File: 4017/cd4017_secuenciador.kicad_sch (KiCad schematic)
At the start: 20 parts, among them J1 CLK_IN_555, J2 ALIM_EXT, J3 POT1_EXT, J4 POT2_EXT, J5 POT3_EXT, J6 POT4_EXT, J7 JACK_OUT, U1 CD4017BE

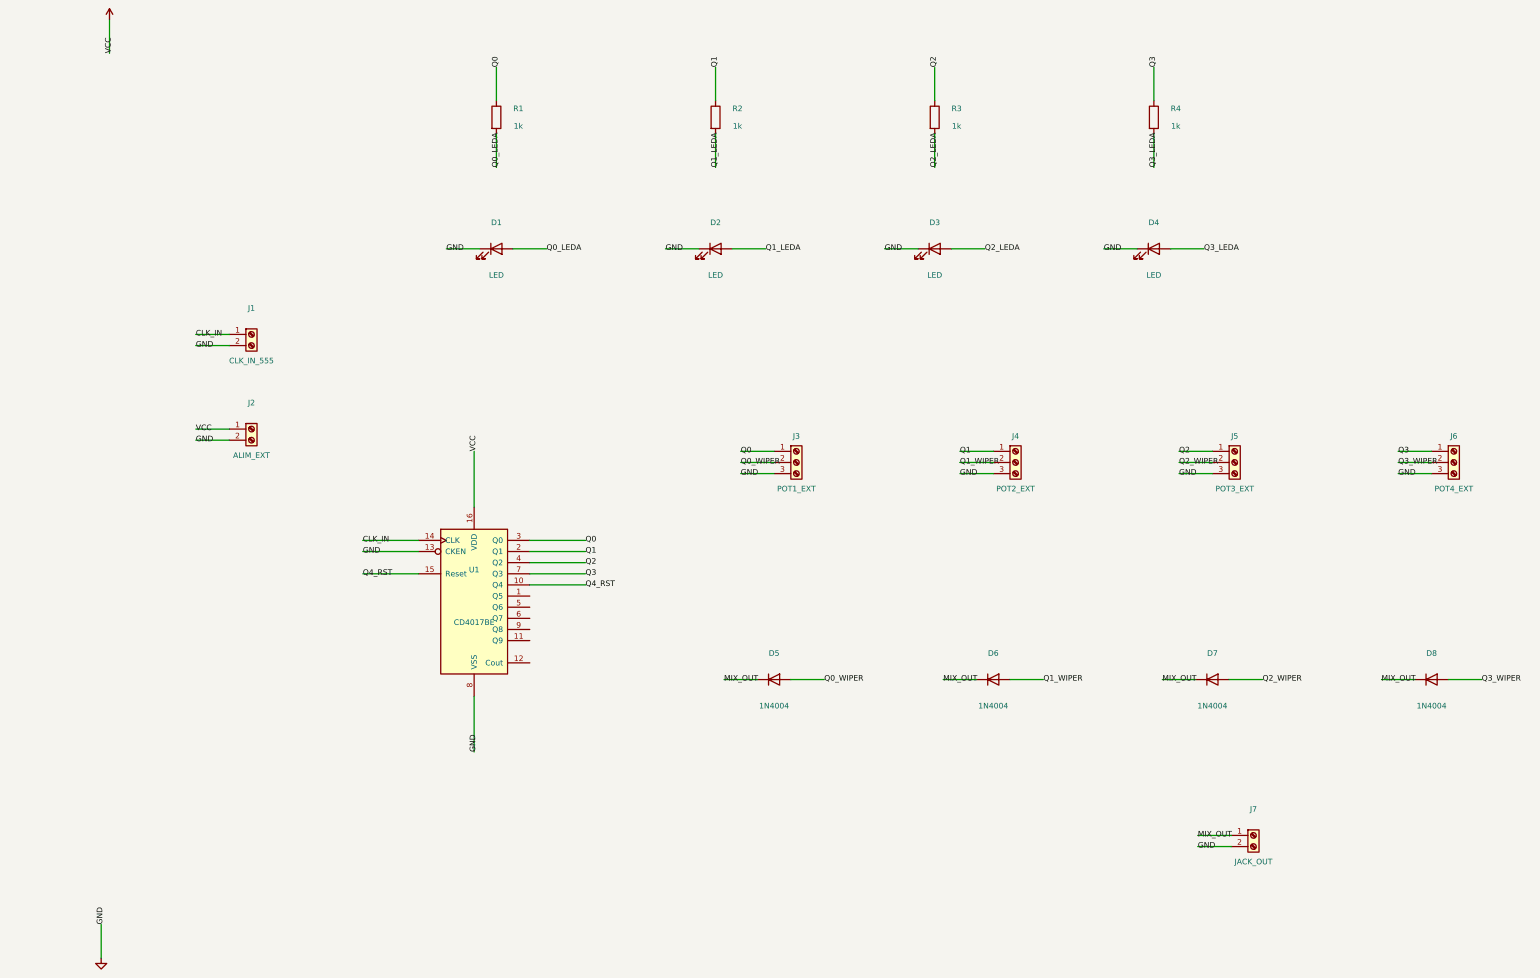
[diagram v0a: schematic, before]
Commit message: enrutado 4017 + correccion esquematico
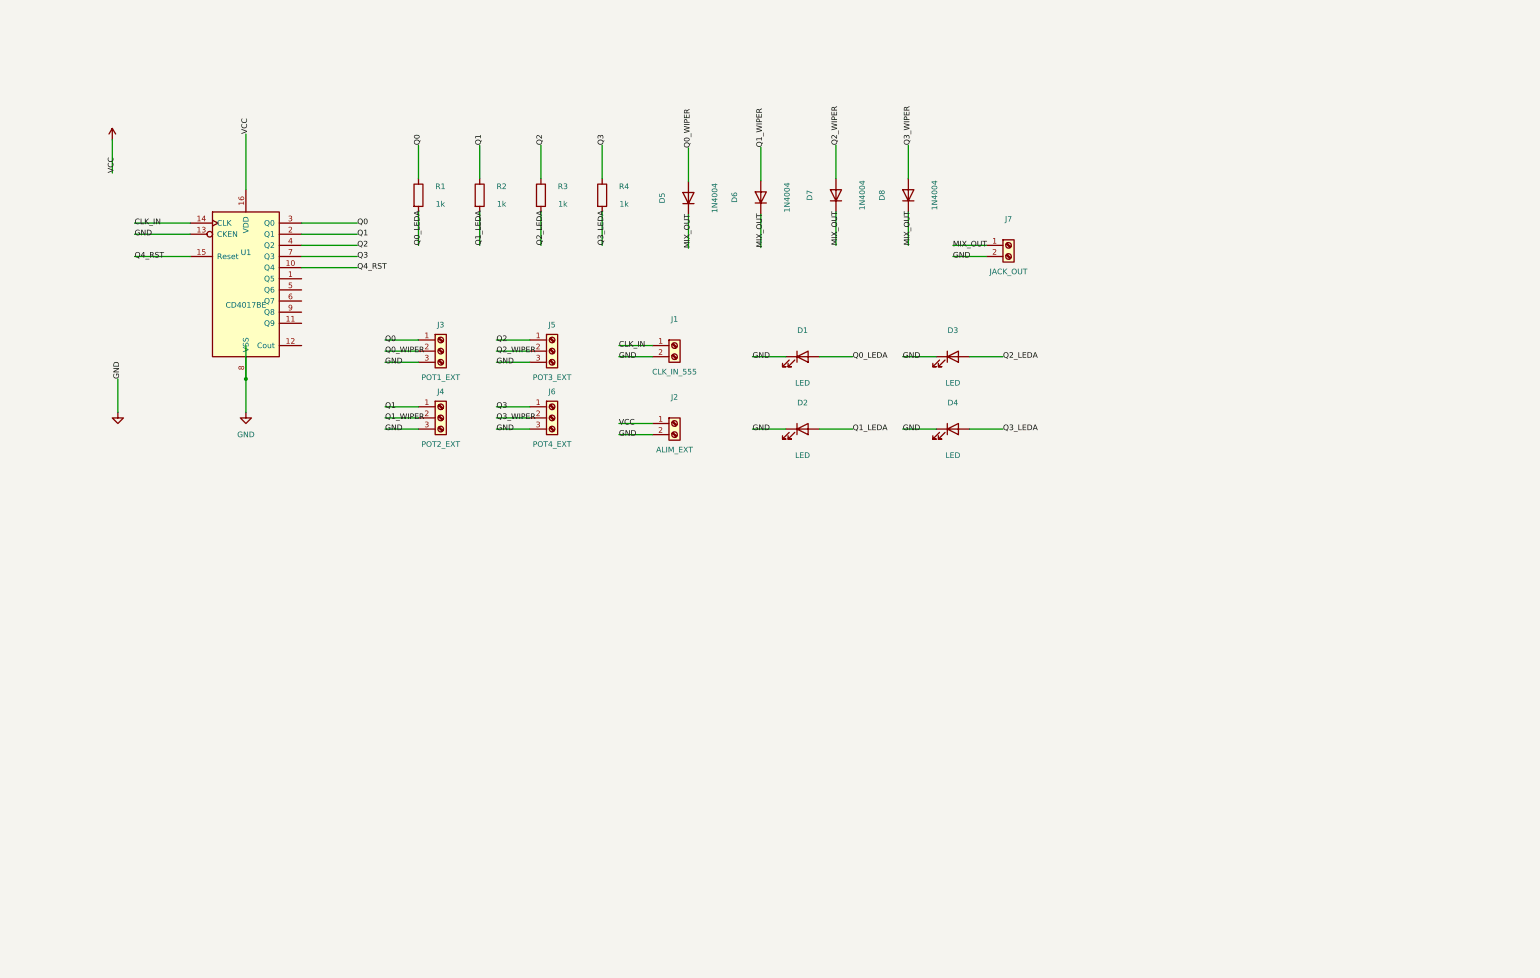
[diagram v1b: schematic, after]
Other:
- moved on the sheet: D1, D2, D3, D4, D5, D6, D7, D8, J1, J2, J3, J4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

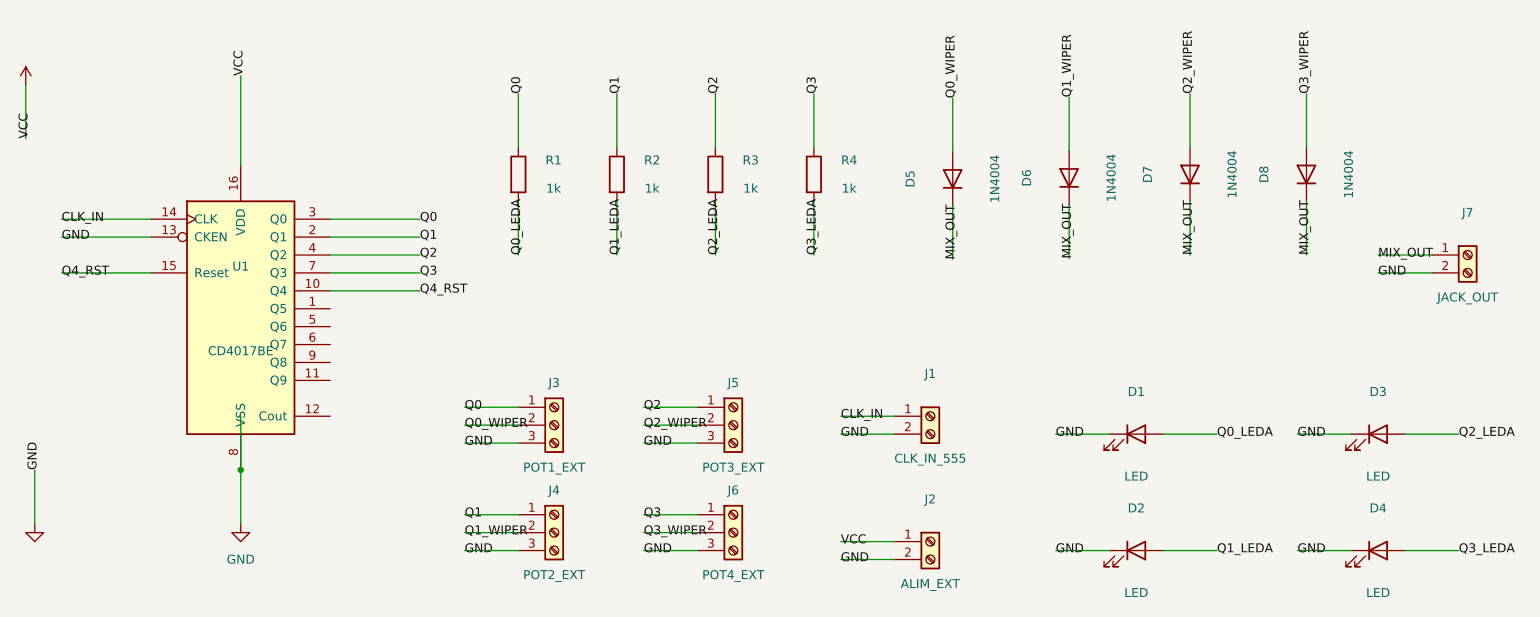
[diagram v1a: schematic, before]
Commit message: fix 555 + design 4017
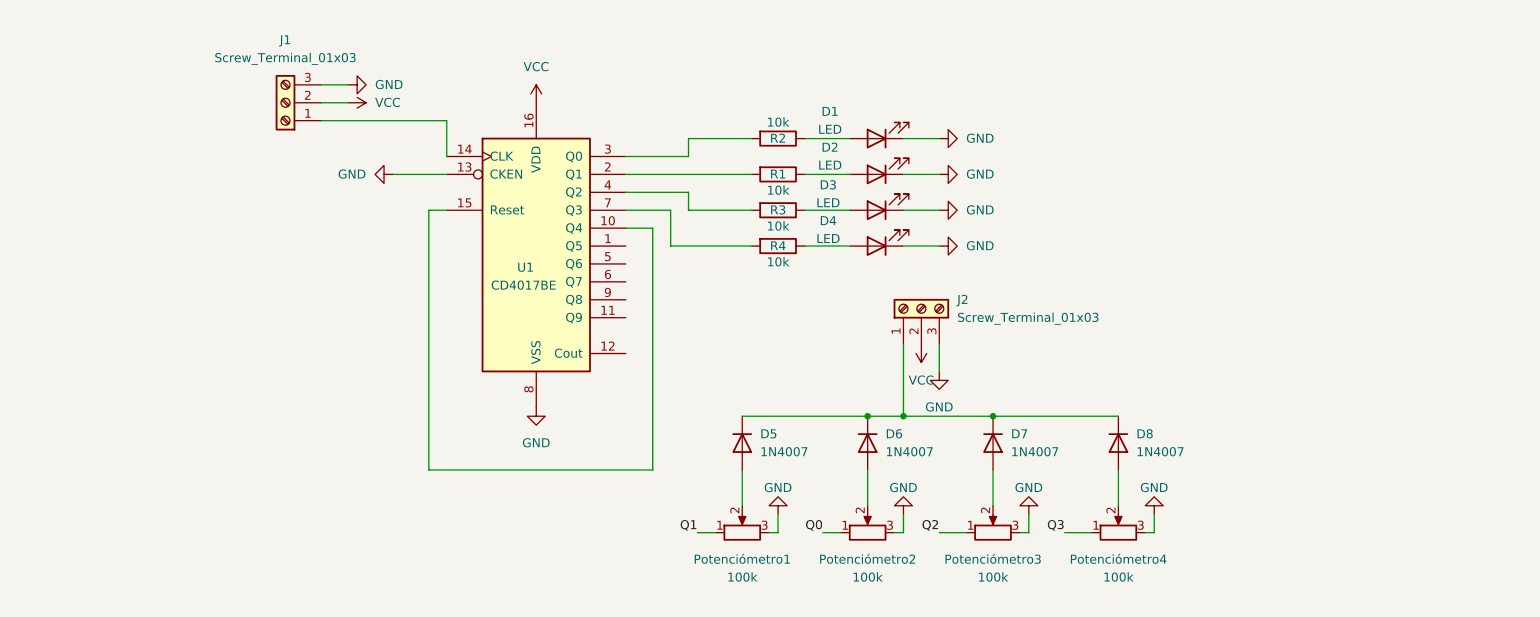
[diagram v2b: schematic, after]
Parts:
- removed D5, D6, D7, D8: 1N4004, Diode_THT:D_DO-41_SOD81_P10.16mm_Horizontal, symbol Diode:1N4001
- removed J1: CLK_IN_555, Connector_PinHeader_2.54mm:PinHeader_1x02_P2.54mm_Vertical, symbol Connector:Screw_Terminal_01x02
- removed J2: ALIM_EXT, TerminalBlock:TerminalBlock_bornier-2_P5.08mm, symbol Connector:Screw_Terminal_01x02
- removed J3: POT1_EXT, TerminalBlock:TerminalBlock_bornier-3_P5.08mm, symbol Connector:Screw_Terminal_01x03
- removed J4: POT2_EXT, TerminalBlock:TerminalBlock_bornier-3_P5.08mm, symbol Connector:Screw_Terminal_01x03
- removed J5: POT3_EXT, TerminalBlock:TerminalBlock_bornier-3_P5.08mm, symbol Connector:Screw_Terminal_01x03
- removed J6: POT4_EXT, TerminalBlock:TerminalBlock_bornier-3_P5.08mm, symbol Connector:Screw_Terminal_01x03
- removed J7: JACK_OUT, Connector_PinHeader_2.54mm:PinHeader_1x02_P2.54mm_Vertical, symbol Connector:Screw_Terminal_01x02
- added D5, D6, D7, D8: 1N4007, Diode_THT:D_DO-41_SOD81_P10.16mm_Horizontal, symbol Diode:1N4007
- added J1, J2: Screw_Terminal_01x03, TerminalBlock_MaiXu_MX126-5.0-03P_1x03_P5.00mm, symbol Connector:Screw_Terminal_01x03
- added Potenciómetro1, Potenciómetro2, Potenciómetro3, Potenciómetro4: 100k, TerminalBlock_MaiXu_MX126-5.0-03P_1x03_P5.00mm, symbol Device:R_Potentiometer
- D1, D2, D3, D4: footprint LED_THT:LED_D5.0mm -> LED_D5.0mm
- R1, R2, R3, R4: value 1k -> 10k; footprint Resistor_THT:R_Axial_DIN0207_L6.3mm_D2.5mm_P10.16mm_Horizontal -> R_Axial_DIN0207_L6.3mm_D2.5mm_P10.16mm_Horizontal
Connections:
- net GND: now also J1.3 (Pin_3), J2.3 (Pin_3), Potenciómetro1.3, Potenciómetro2.3, Potenciómetro3.3, Potenciómetro4.3
- net Q0: now also Potenciómetro2.1; no longer R1.1, U1.3 (Q0)
- net Q1: now also Potenciómetro1.1; no longer R2.1, U1.2 (Q1)
- net Q2: now also Potenciómetro3.1; no longer R3.1, U1.4 (Q2)
- net Q3: now also Potenciómetro4.1; no longer R4.1, U1.7 (Q3)
- net VCC: now also J1.2 (Pin_2), J2.2 (Pin_2)
- net CLK_IN: no longer names the net of U1.14 (CLK)
- net CLK_IN: now also J1.1 (Pin_1)
- net Q0_LEDA: no longer names the net of R1.2
- net Q0_LEDA: now also U1.2 (Q1); no longer D1.2 (A)
- net Q1_LEDA: no longer names the net of D2.2 (A)
- net Q1_LEDA: now also R1.1; no longer R2.2
- net Q2_LEDA: no longer names the net of D3.2 (A)
- net Q2_LEDA: now also R3.1; no longer R3.2
- net Q3_LEDA: no longer names the net of D4.2 (A)
- net Q3_LEDA: now also R4.1; no longer R4.2
- net Q4_RST: no longer names the net of U1.10 (Q4), U1.15 (Reset)
- new net: D5.1 (K), D6.1 (K), D7.1 (K), D8.1 (K), J2.1 (Pin_1)
- new net: D8.2 (A), Potenciómetro4.2
- new net: D1.2 (A), R2.1
- new net: D5.2 (A), Potenciómetro1.2
- new net: D7.2 (A), Potenciómetro3.2
- new net: D6.2 (A), Potenciómetro2.2
- new net: R3.2, U1.4 (Q2)
- new net: R2.2, U1.3 (Q0)
- new net: R4.2, U1.7 (Q3)
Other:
- moved on the sheet: U1

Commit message: arreglar 4017 + iniciar 4093
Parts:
- D1, D2, D3, D4: footprint LED_D5.0mm -> LED_THT:LED_D5.0mm
- J1, J2: footprint TerminalBlock_MaiXu_MX126-5.0-03P_1x03_P5.00mm -> TerminalBlock:TerminalBlock_MaiXu_MX126-5.0-03P_1x03_P5.00mm
- R1: renamed from R2; footprint R_Axial_DIN0207_L6.3mm_D2.5mm_P10.16mm_Horizontal -> Resistor_THT:R_Axial_DIN0207_L6.3mm_D2.5mm_P10.16mm_Horizontal
- R2: renamed from R1; footprint R_Axial_DIN0207_L6.3mm_D2.5mm_P10.16mm_Horizontal -> Resistor_THT:R_Axial_DIN0207_L6.3mm_D2.5mm_P10.16mm_Horizontal
- R3, R4: footprint R_Axial_DIN0207_L6.3mm_D2.5mm_P10.16mm_Horizontal -> Resistor_THT:R_Axial_DIN0207_L6.3mm_D2.5mm_P10.16mm_Horizontal
- RV1: renamed from Potenciómetro1; footprint TerminalBlock_MaiXu_MX126-5.0-03P_1x03_P5.00mm -> TerminalBlock:TerminalBlock_MaiXu_MX126-5.0-03P_1x03_P5.00mm
- RV2: renamed from Potenciómetro2; footprint TerminalBlock_MaiXu_MX126-5.0-03P_1x03_P5.00mm -> TerminalBlock:TerminalBlock_MaiXu_MX126-5.0-03P_1x03_P5.00mm
- RV3: renamed from Potenciómetro3; footprint TerminalBlock_MaiXu_MX126-5.0-03P_1x03_P5.00mm -> TerminalBlock:TerminalBlock_MaiXu_MX126-5.0-03P_1x03_P5.00mm
- RV4: renamed from Potenciómetro4; footprint TerminalBlock_MaiXu_MX126-5.0-03P_1x03_P5.00mm -> TerminalBlock:TerminalBlock_MaiXu_MX126-5.0-03P_1x03_P5.00mm
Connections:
- net Q0: now also R1.2, RV1.1, U1.3 (Q0); no longer RV2.1
- net Q1: now also R2.2, RV2.1, U1.2 (Q1); no longer RV1.1
- net Q2: now also R3.2, U1.4 (Q2)
- net Q3: now also R4.2, U1.7 (Q3)
- no-connect marks 0 -> 6
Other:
- note added: "U1 (4017): 1: sin conexión 2: a R2 a D2 a GND (+), Q1 a patita 1 de RV2 3: a R1 a D1 a GND (+), Q0 a patita 1 de RV1 4: a R3 a D3 a GND (+), Q2 a patita 1 de RV3 5: sin conexión 6: sin conexión 7: a R4 a D4 a GND (+), etiqueta Q3 a patita 1 de RV4 8: a GND (+) 9: sin conexión 10: a pin 15 (Reset) 11: sin conexión 12: sin conexión 13: a GND (+) 14: a J1 pin 1 15: a pin 10 (Q4) 16: a VCC (-) RV1: 1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"
- moved on the sheet: D1, D2, D3, D4, D5, D6, D7, D8, J1, J2, R1, R2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

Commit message: gerbers + correcciones
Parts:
- added H1, H2: MountingHole, symbol Mechanical:MountingHole
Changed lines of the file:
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@@
 	(wire
 		(pts
-			(xy 163.83 57.15) (xy 161.29 57.15)
-		)
-		(stroke
-			(width 0)
-			(type default)
-		)
-	)
-	(wire
-		(pts
 			(xy 190.5 113.03) (xy 190.5 118.11)
 		)
@@
 	(wire
 		(pts
-			(xy 165.1 109.22) (xy 161.29 109.22)
-		)
-		(stroke
-			(width 0)
-			(type default)
-		)
-	)
-	(wire
-		(pts
 			(xy 180.34 81.28) (xy 191.77 81.28)
 		)
@@
 	(wire
 		(pts
-			(xy 161.29 57.15) (xy 161.29 60.96)
+			(xy 161.29 48.26) (xy 161.29 60.96)
 		)
 		(stroke
@@
 	(wire
 		(pts
+			(xy 161.29 104.14) (xy 161.29 106.68)
+		)
+		(stroke
+			(width 0)
+			(type default)
+		)
+	)
+	(wire
+		(pts
 			(xy 184.15 121.92) (xy 186.69 121.92)
 		)
@@
 	(wire
 		(pts
-			(xy 161.29 109.22) (xy 161.29 104.14)
-		)
-		(stroke
-			(width 0)
-			(type default)
-		)
-	)
-	(wire
-		(pts
-			(xy 165.1 109.22) (xy 165.1 104.14)
-		)
-		(stroke
-			(width 0)
-			(type default)
-		)
-	)
-	(wire
-		(pts
 			(xy 182.88 66.04) (xy 191.77 66.04)
 		)
@@
 	(wire
 		(pts
-			(xy 163.83 60.96) (xy 163.83 57.15)
-		)
-		(stroke
-			(width 0)
-			(type default)
-		)
-	)
-	(wire
-		(pts
 			(xy 177.8 113.03) (xy 177.8 78.74)
 		)
@@
 	)
 	(symbol
-		(lib_id "power:VCC")
-		(at 163.83 60.96 180)
-		(unit 1)
-		(body_style 1)
-		(exclude_from_sim no)
-		(in_bom yes)
-		(on_board yes)
-		(in_pos_files yes)
-		(dnp no)
-		(property "Reference" "#PWR01"
-			(at 163.83 57.15 0)
-			(hide yes)
-			(show_name no)
-			(do_not_autoplace no)
-			(effects
-				(font
-					(size 1.27 1.27)
-				)
-			)
-		)
-		(property "Value" "VCC"
-			(at 165.608 62.23 0)
-			(show_name no)
-			(do_not_autoplace no)
-			(effects
-				(font
-					(size 1.27 1.27)
-				)
-				(justify right)
-			)
-		)
-		(property "Footprint" ""
-			(at 163.83 60.96 0)
-			(hide yes)
-			(show_name no)
-			(do_not_autoplace no)
-			(effects
-				(font
-					(size 1.27 1.27)
-				)
-			)
-		)
-		(property "Datasheet" ""
-			(at 163.83 60.96 0)
-			(hide yes)
-			(show_name no)
-			(do_not_autoplace no)
-			(effects
-				(font
-					(size 1.27 1.27)
-				)
-			)
-		)
-		(property "Description" "Power symbol creates a global label with name \"VCC\""
-			(at 163.83 60.96 0)
-			(hide yes)
-			(show_name no)
-			(do_not_autoplace no)
-			(effects
-				(font
-					(size 1.27 1.27)
-				)
-			)
-		)
-		(pin "1"
-		)
-		(instances
-			(project "cd4017_secuenciador"
-				(path "/40cda735-32bf-44d3-a0af-2273aae2d0a8"
-					(reference "#PWR01")
-					(unit 1)
-				)
-			)
-		)
-	)
-	(symbol
 		(lib_id "Device:R_Potentiometer")
 		(at 226.06 121.92 90)
@@
 		(lib_name "GND_1")
 		(lib_id "power:GND")
-		(at 165.1 104.14 180)
+		(at 161.29 106.68 0)
 		(unit 1)
 		(body_style 1)
@@
 		(fields_autoplaced yes)
 		(property "Reference" "#PWR03"
-			(at 165.1 97.79 0)
+			(at 161.29 113.03 0)
 			(hide yes)
 			(show_name no)
@@
 		)
 		(property "Value" "GND"
-			(at 167.64 102.8699 0)
+			(at 163.83 107.9499 0)
 			(show_name no)
 			(do_not_autoplace no)
@@
 					(size 1.27 1.27)
 				)
-				(justify right)
+				(justify left)
 			)
 		)
 		(property "Footprint" ""
-			(at 165.1 104.14 0)
+			(at 161.29 106.68 0)
 			(hide yes)
 			(show_name no)
@@
 		)
 		(property "Datasheet" ""
-			(at 165.1 104.14 0)
+			(at 161.29 106.68 0)
 			(hide yes)
 			(show_name no)
@@
 		)
 		(property "Description" "Power symbol creates a global label with name \"GND\" , ground"
-			(at 165.1 104.14 0)
+			(at 161.29 106.68 0)
 			(hide yes)
 			(show_name no)
@@
 	)
 	(symbol
+		(lib_id "power:VCC")
+		(at 161.29 48.26 0)
+		(unit 1)
+		(body_style 1)
+		(exclude_from_sim no)
+		(in_bom yes)
+		(on_board yes)
+		(in_pos_files yes)
+		(dnp no)
+		(property "Reference" "#PWR01"
+			(at 161.29 52.07 0)
+			(hide yes)
+			(show_name no)
+			(do_not_autoplace no)
+			(effects
+				(font
+					(size 1.27 1.27)
+				)
+			)
+		)
+		(property "Value" "VCC"
+			(at 159.512 46.99 0)
+			(show_name no)
+			(do_not_autoplace no)
+			(effects
+				(font
+					(size 1.27 1.27)
+				)
+				(justify right)
+			)
+		)
+		(property "Footprint" ""
+			(at 161.29 48.26 0)
+			(hide yes)
+			(show_name no)
+			(do_not_autoplace no)
+			(effects
+				(font
+					(size 1.27 1.27)
+				)
+			)
+		)
+		(property "Datasheet" ""
+			(at 161.29 48.26 0)
+			(hide yes)
+			(show_name no)
+			(do_not_autoplace no)
+			(effects
+				(font
+					(size 1.27 1.27)
+				)
+			)
+		)
+		(property "Description" "Power symbol creates a global label with name \"VCC\""
+			(at 161.29 48.26 0)
+			(hide yes)
+			(show_name no)
+			(do_not_autoplace no)
+			(effects
+				(font
+					(size 1.27 1.27)
+				)
+			)
+		)
+		(pin "1"
+		)
+		(instances
+			(project "cd4017_secuenciador"
+				(path "/40cda735-32bf-44d3-a0af-2273aae2d0a8"
+					(reference "#PWR01")
+					(unit 1)
+				)
+			)
+		)
+	)
+	(symbol
+		(lib_id "Mechanical:MountingHole")
+		(at 48.26 66.04 0)
+		(unit 1)
+		(body_style 1)
+		(exclude_from_sim no)
+		(in_bom no)
+		(on_board yes)
+		(in_pos_files yes)
+		(dnp no)
+		(fields_autoplaced yes)
+		(property "Reference" "H1"
+			(at 50.8 64.7699 0)
+			(show_name no)
+			(do_not_autoplace no)
+			(effects
+				(font
+					(size 1.27 1.27)
+				)
+				(justify left)
+			)
+		)
+		(property "Value" "MountingHole"
+			(at 50.8 67.3099 0)
+			(show_name no)
+			(do_not_autoplace no)
+			(effects
+				(font
+					(size 1.27 1.27)
+				)
+				(justify left)
+			)
+		)
+		(property "Footprint" ""
+			(at 48.26 66.04 0)
+			(hide yes)
+			(show_name no)
+			(do_not_autoplace no)
+			(effects
+				(font
+					(size 1.27 1.27)
+				)
+			)
+		)
+		(property "Datasheet" ""
+			(at 48.26 66.04 0)
+			(hide yes)
+			(show_name no)
+			(do_not_autoplace no)
+			(effects
+				(font
+					(size 1.27 1.27)
+				)
+			)
+		)
+		(property "Description" "Mounting Hole without connection"
+			(at 48.26 66.04 0)
+			(hide yes)
+			(show_name no)
+			(do_not_autoplace no)
+			(effects
+				(font
+					(size 1.27 1.27)
+				)
+			)
+		)
+		(instances
+			(project "cd4017_secuenciador"
+				(path "/40cda735-32bf-44d3-a0af-2273aae2d0a8"
+					(reference "H1")
+					(unit 1)
+				)
+			)
+		)
+	)
+	(symbol
 		(lib_id "power:GND")
 		(at 248.92 119.38 180)
@@
 					(unit 1)
 				)
+			)
+		)
+	)
+	(symbol
+		(lib_id "Mechanical:MountingHole")
+		(at 48.26 73.66 0)
+		(unit 1)
+		(body_style 1)
+		(exclude_from_sim no)
+		(in_bom no)
+		(on_board yes)
+		(in_pos_files yes)
+		(dnp no)
+		(fields_autoplaced yes)
+		(property "Reference" "H2"
+			(at 50.8 72.3899 0)
+			(show_name no)
+			(do_not_autoplace no)
+			(effects
+				(font
+					(size 1.27 1.27)
+				)
+				(justify left)
+			)
+		)
+		(property "Value" "MountingHole"
+			(at 50.8 74.9299 0)
+			(show_name no)
+			(do_not_autoplace no)
+			(effects
+				(font
+					(size 1.27 1.27)
+				)
+				(justify left)
+			)
+		)
+		(property "Footprint" ""
+			(at 48.26 73.66 0)
+			(hide yes)
+			(show_name no)
+			(do_not_autoplace no)
+			(effects
+				(font
+					(size 1.27 1.27)
+				)
+			)
+		)
+		(property "Datasheet" ""
+			(at 48.26 73.66 0)
+			(hide yes)
+			(show_name no)
+			(do_not_autoplace no)
+			(effects
+				(font
+					(size 1.27 1.27)
+				)
+			)
+		)
+		(property "Description" "Mounting Hole without connection"
+			(at 48.26 73.66 0)
+			(hide yes)
+			(show_name no)
+			(do_not_autoplace no)
+			(effects
+				(font
+					(size 1.27 1.27)
+				)
+			)
+		)
+		(instances
+			(project "cd4017_secuenciador"
+				(path "/40cda735-32bf-44d3-a0af-2273aae2d0a8"
+					(reference "H2")
+					(unit 1)
+				)
